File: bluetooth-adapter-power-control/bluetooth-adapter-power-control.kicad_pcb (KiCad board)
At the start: 2 copper layers, 16.4 x 20.6 mm, 14 parts, among them J1 UPDI, J2 Conn_01x07_Socket, Q1 NMOS, U1 ATtiny202-SSNR

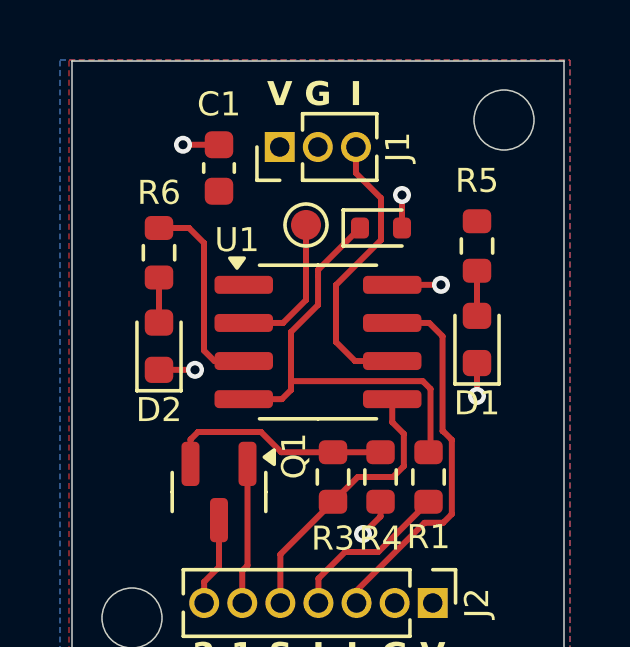
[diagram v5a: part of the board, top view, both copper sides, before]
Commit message: bluetooth-adapter-power-control: add more text to PCB
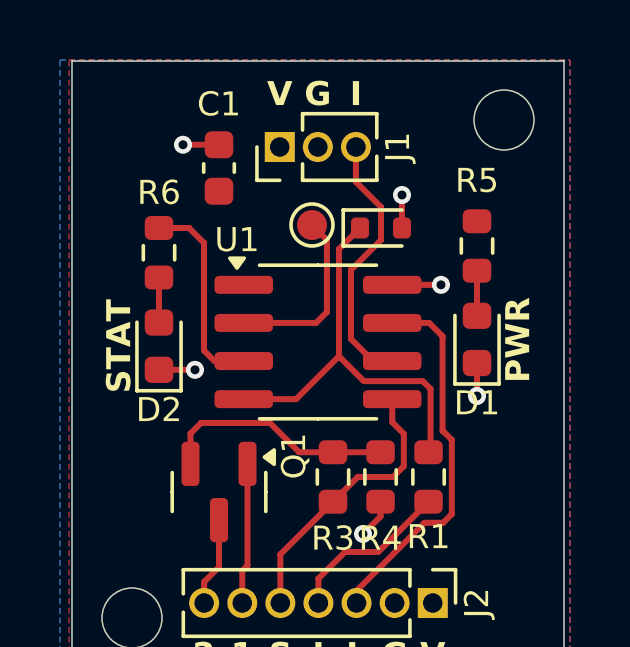
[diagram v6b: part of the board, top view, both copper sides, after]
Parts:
- moved TP1 0.20 mm to (144.8, 62.9)
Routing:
- net Net-(U1-PA6): track 4.89 -> 6.03 mm
- net CAR_ON: track 15.0 -> 14.0 mm
- net UPDI: track 9.61 -> 8.84 mm
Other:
- board text added: "DESIGNED BY RYAN HAUSMANN"
- board text added: "PWR"
- board text added: "STAT"
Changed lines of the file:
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@@
 	(footprint "TestPoint:TestPoint_Pad_D1.0mm"
 		(layer "F.Cu")
-		(at 144.6 62.9)
+		(at 144.8 62.9)
 		(descr "SMD pad as test Point, diameter 1.0mm")
 		(tags "test point SMD pad")
@@
 		(layer "Edge.Cuts")
 	)
+	(gr_text "PWR"
+		(at 151.2 66.735 90)
+		(layer "F.SilkS")
+		(effects
+			(font
+				(size 0.8 0.8)
+				(thickness 0.16)
+				(bold yes)
+			)
+			(justify top)
+		)
+	)
 	(gr_text "I"
 		(at 145.015 77.7 0)
@@
 		)
 	)
+	(gr_text "STAT"
+		(at 137.9 66.94 90)
+		(layer "F.SilkS")
+		(effects
+			(font
+				(size 0.8 0.8)
+				(thickness 0.16)
+				(bold yes)
+			)
+			(justify top)
+		)
+	)
 	(gr_text "I"
 		(at 146.265 59 0)
@@
 		)
 	)
+	(gr_text "DESIGNED BY\nRYAN HAUSMANN"
+		(at 145 67.735 0)
+		(layer "B.SilkS")
+		(effects
+			(font
+				(size 0.8 0.8)
+				(thickness 0.16)
+				(bold yes)
+			)
+			(justify mirror)
+		)
+	)
 	(segment
 		(start 147.085 72.125)
@@
 	)
 	(segment
-		(start 146.265 61.17)
-		(end 146.265 60.3)
+		(start 146.1 64.4)
+		(end 146.1 66.7)
 		(width 0.2)
 		(layer "F.Cu")
@@
 	)
 	(segment
-		(start 145.6 66.8)
-		(end 146.235 67.435)
+		(start 146.265 60.3)
+		(end 146.265 61.465)
 		(width 0.2)
 		(layer "F.Cu")
@@
 	)
 	(segment
-		(start 145.6 64.9)
-		(end 145.6 66.8)
+		(start 147.1 63.4)
+		(end 146.1 64.4)
 		(width 0.2)
 		(layer "F.Cu")
@@
 	)
 	(segment
-		(start 147.1 62.005)
-		(end 146.265 61.17)
+		(start 146.835 67.435)
+		(end 147.475 67.435)
 		(width 0.2)
 		(layer "F.Cu")
@@
 	)
 	(segment
-		(start 147.1 63.4)
-		(end 145.6 64.9)
+		(start 146.1 66.7)
+		(end 146.835 67.435)
 		(width 0.2)
 		(layer "F.Cu")
@@
 	)
 	(segment
-		(start 146.235 67.435)
-		(end 147.475 67.435)
+		(start 146.265 61.465)
+		(end 147.1 62.3)
 		(width 0.2)
 		(layer "F.Cu")
@@
 	)
 	(segment
-		(start 147.1 62.005)
+		(start 147.1 62.3)
 		(end 147.1 63.4)
 		(width 0.2)
@@
 	)
 	(segment
+		(start 148.490968 68.104)
+		(end 148.751 68.364032)
+		(width 0.2)
+		(layer "F.Cu")
+		(net 6)
+	)
+	(segment
+		(start 144.269968 68.705)
+		(end 142.525 68.705)
+		(width 0.2)
+		(layer "F.Cu")
+		(net 6)
+	)
+	(segment
+		(start 146.527032 68.104)
+		(end 148.490968 68.104)
+		(width 0.2)
+		(layer "F.Cu")
+		(net 6)
+	)
+	(segment
+		(start 145.699 67.275968)
+		(end 144.269968 68.705)
+		(width 0.2)
+		(layer "F.Cu")
+		(net 6)
+	)
+	(segment
+		(start 145.699 67.275968)
+		(end 146.527032 68.104)
+		(width 0.2)
+		(layer "F.Cu")
+		(net 6)
+	)
+	(segment
+		(start 146.4 63)
+		(end 145.699 63.701)
+		(width 0.2)
+		(layer "F.Cu")
+		(net 6)
+	)
+	(segment
+		(start 148.751 70.409)
+		(end 148.685 70.475)
+		(width 0.2)
+		(layer "F.Cu")
+		(net 6)
+	)
+	(segment
 		(start 148.751 68.364032)
-		(end 148.490968 68.104)
+		(end 148.751 70.409)
 		(width 0.2)
 		(layer "F.Cu")
@@
 	)
 	(segment
-		(start 145.001 64.399)
-		(end 145.001 64.6)
+		(start 145.699 63.701)
+		(end 145.699 67.275968)
 		(width 0.2)
 		(layer "F.Cu")
@@
 	)
 	(segment
-		(start 144.1 68.4)
-		(end 143.795 68.705)
-		(width 0.2)
-		(layer "F.Cu")
-		(net 6)
-	)
-	(segment
-		(start 148.751 70.409)
-		(end 148.751 68.364032)
-		(width 0.2)
-		(layer "F.Cu")
-		(net 6)
-	)
-	(segment
-		(start 146.4 63)
-		(end 145.001 64.399)
-		(width 0.2)
-		(layer "F.Cu")
-		(net 6)
-	)
-	(segment
-		(start 144.1 68.104)
-		(end 144.1 68.4)
-		(width 0.2)
-		(layer "F.Cu")
-		(net 6)
-	)
-	(segment
-		(start 145.001 65.5661)
-		(end 144.1 66.4671)
-		(width 0.2)
-		(layer "F.Cu")
-		(net 6)
-	)
-	(segment
-		(start 144.1 66.4671)
-		(end 144.1 68.104)
-		(width 0.2)
-		(layer "F.Cu")
-		(net 6)
-	)
-	(segment
-		(start 145.001 64.6)
-		(end 145.001 65.5661)
-		(width 0.2)
-		(layer "F.Cu")
-		(net 6)
-	)
-	(segment
-		(start 148.490968 68.104)
-		(end 144.1 68.104)
-		(width 0.2)
-		(layer "F.Cu")
-		(net 6)
-	)
-	(segment
-		(start 148.685 70.475)
-		(end 148.751 70.409)
-		(width 0.2)
-		(layer "F.Cu")
-		(net 6)
-	)
-	(segment
-		(start 143.795 68.705)
-		(end 142.525 68.705)
-		(width 0.2)
-		(layer "F.Cu")
-		(net 6)
-	)
-	(segment
-		(start 145.5 70.475)
-		(end 143.775 70.475)
+		(start 141.1 69.5)
+		(end 140.75 69.85)
 		(width 0.2)
 		(layer "F.Cu")
@@
 	)
 	(segment
-		(start 140.75 70.05)
+		(start 143.4 69.5)
+		(end 141.1 69.5)
+		(width 0.2)
+		(layer "F.Cu")
+		(net 7)
+	)
+	(segment
+		(start 140.75 69.85)
 		(end 140.75 70.8625)
-		(width 0.2)
-		(layer "F.Cu")
-		(net 7)
-	)
-	(segment
-		(start 143.775 70.475)
-		(end 143.1 69.8)
-		(width 0.2)
-		(layer "F.Cu")
-		(net 7)
-	)
-	(segment
-		(start 143.1 69.8)
-		(end 141 69.8)
-		(width 0.2)
-		(layer "F.Cu")
-		(net 7)
-	)
-	(segment
-		(start 141 69.8)
-		(end 140.75 70.05)
 		(width 0.2)
 		(layer "F.Cu")
@@
 	)
 	(segment
+		(start 145.5 70.475)
+		(end 144.375 70.475)
+		(width 0.2)
+		(layer "F.Cu")
+		(net 7)
+	)
+	(segment
+		(start 144.375 70.475)
+		(end 143.4 69.5)
+		(width 0.2)
+		(layer "F.Cu")
+		(net 7)
+	)
+	(segment
 		(start 142.65 74.25)
 		(end 142.475 74.425)
@@
 	)
 	(segment
+		(start 144.935 66.165)
+		(end 145.298 65.802)
+		(width 0.2)
+		(layer "F.Cu")
+		(net 13)
+	)
+	(segment
 		(start 142.525 66.165)
-		(end 143.835 66.165)
+		(end 144.935 66.165)
 		(width 0.2)
 		(layer "F.Cu")
@@
 	)
 	(segment
-		(start 144.6 65.4)
-		(end 144.6 62.9)
+		(start 145.298 63.398)
+		(end 144.8 62.9)
 		(width 0.2)
 		(layer "F.Cu")
@@
 	)
 	(segment
-		(start 143.835 66.165)
-		(end 144.6 65.4)
-		(width 0.2)
-		(layer "F.Cu")
+		(start 145.298 65.802)
+		(end 145.298 63.398)
+		(width 0.2)
+		(layer "F.Cu")
